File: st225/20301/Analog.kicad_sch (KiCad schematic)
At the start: 108 parts, among them J1 control, J2 data, J4 SPINDLE, J5 HEADS, J7 CONFIG, Q1 BD436, Q13 2N3904, Q2 2N6039, Q3 BD436, Q4 2N6039, Q5 BD436, Q7 2N3904, Q9 2N3906

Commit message: Numerous small changes, README updates
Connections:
- net HDC3: no longer 5F1.8 (C), J5.15 (Pin_15), RP1.6 (R5), RP2.6 (R5)
- new net HDC4: 5F1.8 (C), J5.15 (Pin_15), RP1.6 (R5), RP2.6 (R5)
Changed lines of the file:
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@@
     (effects (font (size 1.27 1.27)) (justify right bottom))
   )
-  (label "HDC3" (at 176.53 101.6 0) (fields_autoplaced)
+  (label "HDC4" (at 176.53 101.6 0) (fields_autoplaced)
     (effects (font (size 1.27 1.27)) (justify left bottom))
   )

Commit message: st225 updates with more info
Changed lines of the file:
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@@
   (junction (at 190.5 63.5) (diameter 0) (color 0 0 0 0)
   )
-  (junction (at 77.47 92.71) (diameter 0) (color 0 0 0 0)
-  )
   (junction (at 257.81 133.35) (diameter 0) (color 0 0 0 0)
   )
@@
   )
   (junction (at 391.16 167.64) (diameter 0) (color 0 0 0 0)
+  )
+  (junction (at 59.69 92.71) (diameter 0) (color 0 0 0 0)
   )
   (junction (at 242.57 101.6) (diameter 0) (color 0 0 0 0)
@@
     (stroke (width 0) (type default))
   )
-  (wire (pts (xy 77.47 92.71) (xy 77.47 48.26))
-    (stroke (width 0) (type default))
-  )
   (wire (pts (xy 158.75 113.03) (xy 158.75 109.22))
     (stroke (width 0) (type default))
@@
     (stroke (width 0) (type default))
   )
+  (wire (pts (xy 77.47 58.42) (xy 77.47 48.26))
+    (stroke (width 0) (type default))
+  )
   (wire (pts (xy 293.37 77.47) (xy 290.83 77.47))
     (stroke (width 0) (type default))
@@
     (stroke (width 0) (type default))
   )
-  (wire (pts (xy 34.29 92.71) (xy 77.47 92.71))
+  (wire (pts (xy 34.29 92.71) (xy 59.69 92.71))
     (stroke (width 0) (type default))
   )
@@
     (stroke (width 0) (type default))
   )
+  (wire (pts (xy 59.69 92.71) (xy 59.69 58.42))
+    (stroke (width 0) (type default))
+  )
   (wire (pts (xy 95.25 175.26) (xy 92.71 175.26))
     (stroke (width 0) (type default))
@@
     (stroke (width 0) (type default))
   )
+  (wire (pts (xy 59.69 58.42) (xy 77.47 58.42))
+    (stroke (width 0) (type default))
+  )
   (wire (pts (xy 386.08 212.09) (xy 391.16 212.09))
     (stroke (width 0) (type default))
@@
   )
   (wire (pts (xy 241.3 87.63) (xy 243.84 87.63))
+    (stroke (width 0) (type default))
+  )
+  (wire (pts (xy 59.69 92.71) (xy 77.47 92.71))
     (stroke (width 0) (type default))
   )
@@
     )
   )
-  (symbol (lib_id "st225:MPQ2907") (at 153.67 58.42 0) (unit 1)
+  (symbol (lib_id "st225:MPQ2907") (at 153.67 58.42 0) (mirror x) (unit 1)
     (in_bom yes) (on_board yes) (dnp no)
     (property "Reference" "5F1" (at 158.75 58.42 0)

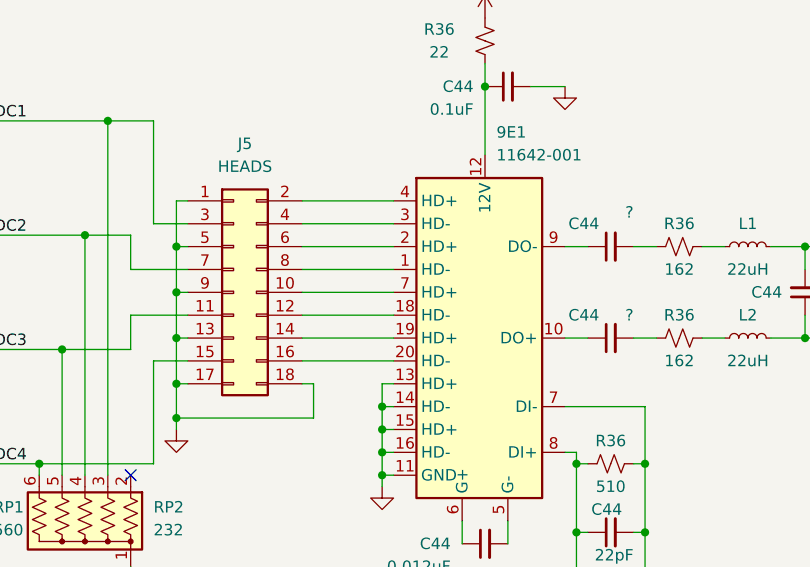
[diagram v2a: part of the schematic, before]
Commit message: Fix missing connection on 20301 head
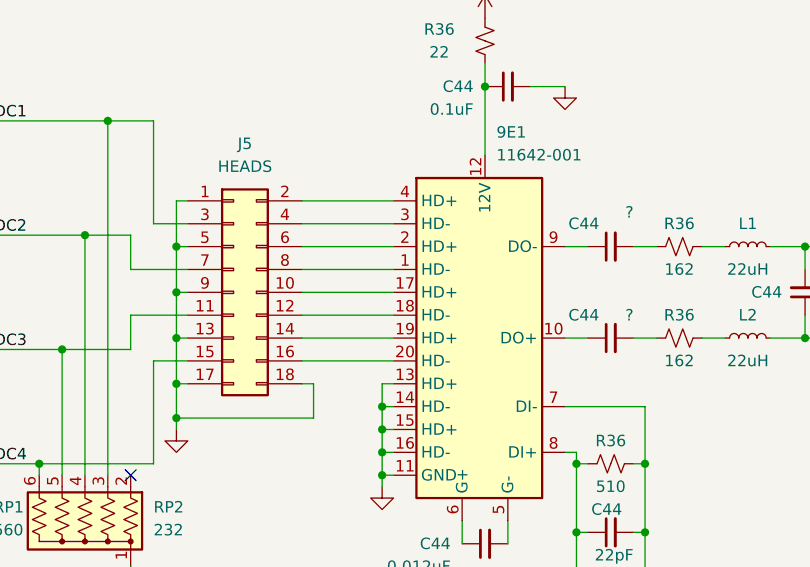
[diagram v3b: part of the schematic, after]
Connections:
- net at J5.10 (Pin_10): now also 9E1.17 (HD+); no longer 9E1.7 (HD+)
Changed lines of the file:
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@@
     (pin "15")
     (pin "16")
+    (pin "17")
     (pin "18")
     (pin "19")
@@
     (pin "6")
     (pin "7")
-    (pin "7")
     (pin "8")
